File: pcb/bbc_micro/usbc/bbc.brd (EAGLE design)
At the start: 43 x 34.7 mm, 29 parts, among them U2 LM2776

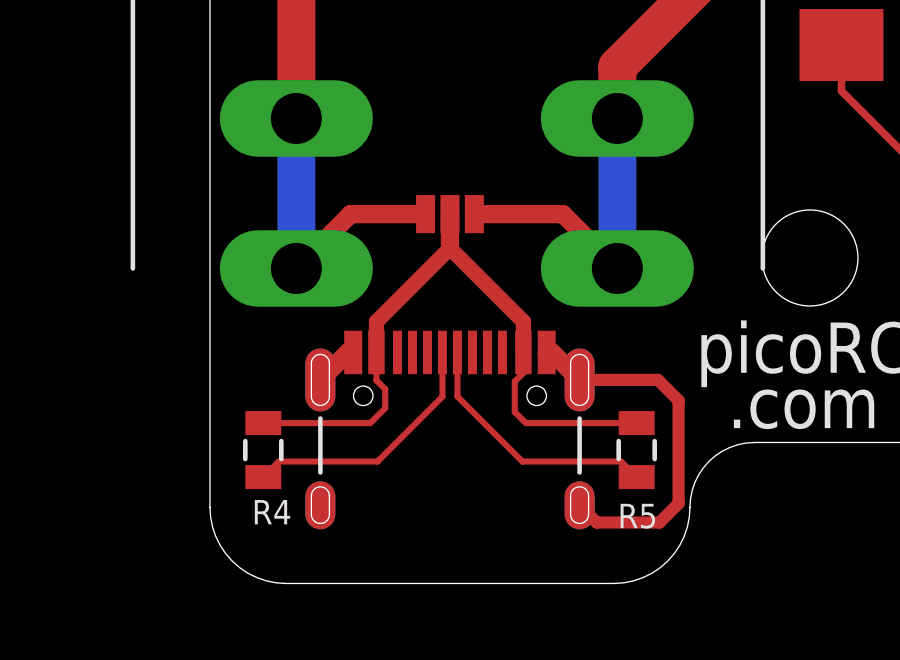
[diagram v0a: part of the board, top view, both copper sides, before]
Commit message: adjusted jumper angle, fixed pin bug
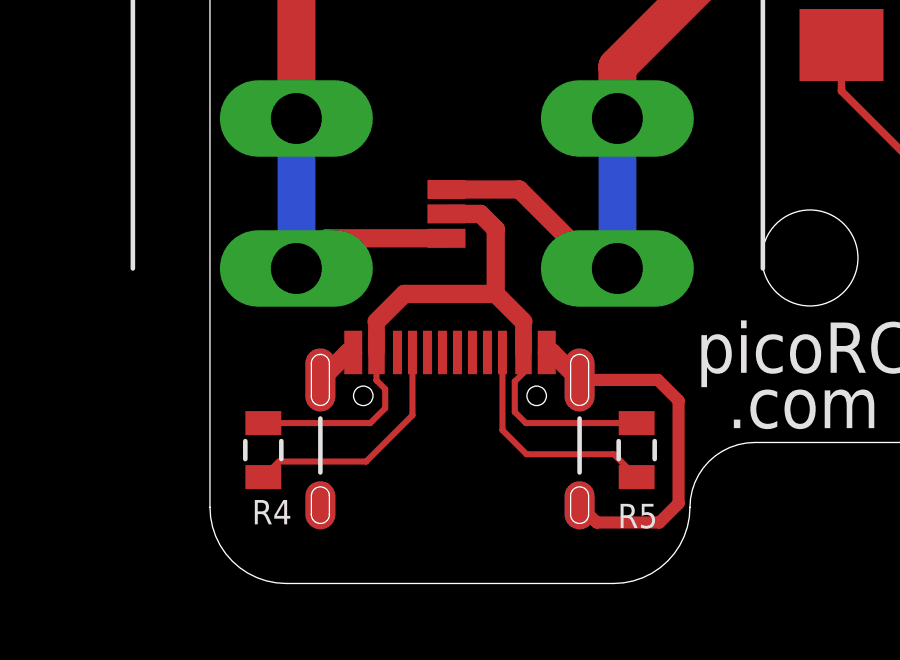
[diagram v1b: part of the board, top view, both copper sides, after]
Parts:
- moved JP1 0.12 mm to (7.88, 7.62), turned to 90 degrees
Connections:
- net N$8: now also J1.B5, R5.2; no longer J1.A6, J1.B6, R4.2
- net N$9: now also J1.A5, R4.2; no longer J1.A7, J1.B7, R5.2
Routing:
- net N$5: track 22.7 -> 24.3 mm
- net +5V: track 65.9 -> 67.2 mm
- net N$8: track 8.56 -> 7.71 mm
- net N$9: track 8.56 -> 7.92 mm
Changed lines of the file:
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@@
 <layer number="14" name="Route14" color="22" fill="1" visible="no" active="no"/>
 <layer number="15" name="Route15" color="23" fill="1" visible="no" active="no"/>
-<layer number="16" name="Bottom" color="1" fill="1" visible="no" active="yes"/>
+<layer number="16" name="Bottom" color="1" fill="1" visible="yes" active="yes"/>
 <layer number="17" name="Pads" color="2" fill="1" visible="yes" active="yes"/>
 <layer number="18" name="Vias" color="2" fill="1" visible="yes" active="yes"/>
 <layer number="19" name="Unrouted" color="6" fill="1" visible="yes" active="yes"/>
 <layer number="20" name="Dimension" color="24" fill="1" visible="yes" active="yes"/>
-<layer number="21" name="tPlace" color="7" fill="1" visible="yes" active="yes"/>
+<layer number="21" name="tPlace" color="7" fill="1" visible="no" active="yes"/>
 <layer number="22" name="bPlace" color="7" fill="1" visible="no" active="yes"/>
 <layer number="23" name="tOrigins" color="15" fill="1" visible="yes" active="yes"/>
-<layer number="24" name="bOrigins" color="15" fill="1" visible="no" active="yes"/>
-<layer number="25" name="tNames" color="7" fill="1" visible="yes" active="yes"/>
+<layer number="24" name="bOrigins" color="15" fill="1" visible="yes" active="yes"/>
+<layer number="25" name="tNames" color="7" fill="1" visible="no" active="yes"/>
 <layer number="26" name="bNames" color="7" fill="1" visible="no" active="yes"/>
 <layer number="27" name="tValues" color="7" fill="1" visible="no" active="yes"/>
@@
 <layer number="29" name="tStop" color="7" fill="3" visible="no" active="yes"/>
 <layer number="30" name="bStop" color="7" fill="6" visible="no" active="yes"/>
-<layer number="31" name="tCream" color="7" fill="4" visible="no" active="yes"/>
+<layer number="31" name="tCream" color="7" fill="4" visible="yes" active="yes"/>
 <layer number="32" name="bCream" color="7" fill="5" visible="no" active="yes"/>
 <layer number="33" name="tFinish" color="6" fill="3" visible="no" active="yes"/>
@@
 <layer number="38" name="bTest" color="7" fill="1" visible="no" active="yes"/>
 <layer number="39" name="tKeepout" color="4" fill="11" visible="yes" active="yes"/>
-<layer number="40" name="bKeepout" color="1" fill="11" visible="no" active="yes"/>
+<layer number="40" name="bKeepout" color="1" fill="11" visible="yes" active="yes"/>
 <layer number="41" name="tRestrict" color="4" fill="10" visible="yes" active="yes"/>
-<layer number="42" name="bRestrict" color="1" fill="10" visible="no" active="yes"/>
+<layer number="42" name="bRestrict" color="1" fill="10" visible="yes" active="yes"/>
 <layer number="43" name="vRestrict" color="2" fill="10" visible="no" active="yes"/>
 <layer number="44" name="Drills" color="7" fill="1" visible="yes" active="yes"/>
@@
 <layer number="49" name="Reference" color="7" fill="1" visible="no" active="yes"/>
 <layer number="50" name="dxf" color="7" fill="1" visible="no" active="no"/>
-<layer number="51" name="tDocu" color="7" fill="1" visible="yes" active="yes"/>
+<layer number="51" name="tDocu" color="7" fill="1" visible="no" active="yes"/>
 <layer number="52" name="bDocu" color="7" fill="1" visible="no" active="yes"/>
 <layer number="53" name="tGND_GNDA" color="7" fill="1" visible="no" active="no"/>
@@
 <text x="34.871" y="1.211" size="1.6764" layer="25" distance="35" align="center">G</text>
 <polygon width="0.2032" layer="41">
-<vertex x="6.604" y="9.652"/>
-<vertex x="9.017" y="9.652"/>
+<vertex x="6.985" y="9.398"/>
+<vertex x="9.271" y="9.398"/>
 <vertex x="10.16" y="8.509"/>
 <vertex x="10.16" y="6.731"/>
-<vertex x="9.398" y="5.969"/>
-<vertex x="6.35" y="5.969"/>
-<vertex x="5.461" y="6.858"/>
-<vertex x="5.461" y="8.509"/>
+<vertex x="9.525" y="6.096"/>
+<vertex x="6.858" y="6.096"/>
+<vertex x="6.223" y="6.731"/>
+<vertex x="6.223" y="8.636"/>
 </polygon>
 <text x="32.204" y="10.609" size="1.4224" layer="25" distance="35" align="center">G</text>
@@
 <attribute name="VALUE" x="8" y="-0.81" size="0.762" layer="27" align="center"/>
 </element>
-<element name="JP1" library="SparkFun-Jumpers" package="SMT-JUMPER_3_1-NC_PASTE_NO-SILK" value="JUMPER-SMT_3_1-NC_PASTE_NO-SILK" x="8" y="7.611" smashed="yes"/>
+<element name="JP1" library="SparkFun-Jumpers" package="SMT-JUMPER_3_1-NC_PASTE_NO-SILK" value="JUMPER-SMT_3_1-NC_PASTE_NO-SILK" x="7.883" y="7.619" smashed="yes" rot="R90"/>
 <element name="R4" library="atx_power_control" package="0805" value="10K" x="1.778" y="-0.254" smashed="yes" rot="R270">
 <attribute name="NAME" x="1.397" y="-2.7305" size="0.8128" layer="25"/>
@@
 <wire x1="31.096" y1="2.356" x2="32.3" y2="3.56" width="1.016" layer="1"/>
 <contactref element="JP1" pad="3"/>
-<wire x1="8.8128" y1="7.611" x2="11.769" y2="7.611" width="0.6096" layer="1"/>
-<wire x1="11.769" y1="7.611" x2="13.58" y2="5.8" width="0.6096" layer="1"/>
+<wire x1="7.883" y1="8.4318" x2="10.3132" y2="8.4318" width="0.6096" layer="1"/>
+<wire x1="12.945" y1="5.8" x2="13.58" y2="5.8" width="0.6096" layer="1"/>
+<wire x1="12.945" y1="5.8" x2="10.3132" y2="8.4318" width="0.6096" layer="1"/>
 </signal>
 <signal name="N$31">
@@
 <wire x1="7.183" y1="19.549" x2="2.88" y2="15.246" width="1.27" layer="1"/>
 <contactref element="JP1" pad="1"/>
-<wire x1="2.88" y1="5.8" x2="4.691" y2="7.611" width="0.6096" layer="1"/>
-<wire x1="4.691" y1="7.611" x2="7.1872" y2="7.611" width="0.6096" layer="1"/>
+<wire x1="2.88" y1="5.8" x2="3.8862" y2="6.8062" width="0.6096" layer="1"/>
+<wire x1="3.8862" y1="6.8062" x2="7.883" y2="6.8062" width="0.6096" layer="1"/>
 </signal>
 <signal name="N$6">
@@
 <contactref element="J1" pad="VBUS2"/>
 <contactref element="J1" pad="VBUS1"/>
-<wire x1="5.55" y1="3" x2="5.55" y2="4.026" width="0.508" layer="1"/>
-<wire x1="8" y1="6.476" x2="8" y2="6.477" width="0.508" layer="1"/>
-<wire x1="8" y1="6.477" x2="8" y2="6.604" width="0.508" layer="1"/>
-<wire x1="8" y1="6.604" x2="8" y2="7.611" width="0.6096" layer="1"/>
-<wire x1="5.55" y1="4.026" x2="8" y2="6.476" width="0.508" layer="1"/>
-<wire x1="10.45" y1="3" x2="10.45" y2="4.027" width="0.508" layer="1"/>
-<wire x1="10.45" y1="4.027" x2="8" y2="6.477" width="0.508" layer="1"/>
+<wire x1="5.55" y1="4.026" x2="5.55" y2="3" width="0.5588" layer="1"/>
+<wire x1="10.45" y1="4.027" x2="10.45" y2="3" width="0.5588" layer="1"/>
 <contactref element="R5" pad="1"/>
 <contactref element="R4" pad="1"/>
@@
 <wire x1="10.45" y1="2.322" x2="10.45" y2="3" width="0.2032" layer="1"/>
 <wire x1="10.53" y1="0.646" x2="10.16" y2="1.016" width="0.2032" layer="1"/>
+<wire x1="7.883" y1="7.619" x2="9.018" y2="7.619" width="0.6096" layer="1"/>
+<wire x1="9.018" y1="7.619" x2="9.525" y2="7.112" width="0.6096" layer="1"/>
+<wire x1="9.525" y1="7.112" x2="9.525" y2="4.952" width="0.6096" layer="1"/>
+<wire x1="9.525" y1="4.952" x2="10.45" y2="4.027" width="0.6096" layer="1"/>
+<wire x1="9.525" y1="4.952" x2="6.476" y2="4.952" width="0.6096" layer="1"/>
+<wire x1="6.476" y1="4.952" x2="5.55" y2="4.026" width="0.6096" layer="1"/>
 </signal>
 <signal name="N$8">
-<contactref element="J1" pad="A6" route="any" routetag="J1.D+"/>
-<contactref element="J1" pad="B6" route="any" routetag="J1.D+"/>
+<contactref element="R5" pad="2"/>
+<contactref element="J1" pad="B5"/>
+<wire x1="14.224" y1="-1.154" x2="13.462" y2="-0.392" width="0.2032" layer="1"/>
+<wire x1="13.462" y1="-0.392" x2="10.552" y2="-0.392" width="0.2032" layer="1"/>
+<wire x1="9.75" y1="0.41" x2="9.75" y2="3" width="0.2032" layer="1"/>
+<wire x1="10.552" y1="-0.392" x2="9.75" y2="0.41" width="0.2032" layer="1"/>
+</signal>
+<signal name="N$9">
 <contactref element="R4" pad="2"/>
-<wire x1="1.778" y1="-1.154" x2="2.297" y2="-0.635" width="0.2032" layer="1"/>
-<wire x1="7.75" y1="1.527" x2="7.75" y2="3" width="0.2032" layer="1"/>
-<wire x1="2.297" y1="-0.635" x2="5.588" y2="-0.635" width="0.2032" layer="1"/>
-<wire x1="5.588" y1="-0.635" x2="7.75" y2="1.527" width="0.2032" layer="1"/>
-</signal>
-<signal name="N$9">
-<contactref element="J1" pad="A7"/>
-<contactref element="J1" pad="B7"/>
-<contactref element="R5" pad="2"/>
-<wire x1="14.224" y1="-1.154" x2="13.705" y2="-0.635" width="0.2032" layer="1"/>
-<wire x1="8.25" y1="1.529" x2="8.25" y2="3" width="0.2032" layer="1"/>
-<wire x1="13.705" y1="-0.635" x2="10.414" y2="-0.635" width="0.2032" layer="1"/>
-<wire x1="10.414" y1="-0.635" x2="8.25" y2="1.529" width="0.2032" layer="1"/>
-<wire x1="8.25" y1="3" x2="7.25" y2="3" width="0" layer="19" extent="1-1"/>
+<contactref element="J1" pad="A5"/>
+<wire x1="6.75" y1="3" x2="6.75" y2="0.908" width="0.2032" layer="1"/>
+<wire x1="2.297" y1="-0.635" x2="1.778" y2="-1.154" width="0.2032" layer="1"/>
+<wire x1="6.75" y1="0.908" x2="5.207" y2="-0.635" width="0.2032" layer="1"/>
+<wire x1="5.207" y1="-0.635" x2="2.297" y2="-0.635" width="0.2032" layer="1"/>
 </signal>
 </signals>
@@
 <mfgpreviewcolor name="substratecolor" color="0xFF786E46"/>
 </mfgpreviewcolors>
+<errors>
+</errors>
 </board>
 </drawing>
